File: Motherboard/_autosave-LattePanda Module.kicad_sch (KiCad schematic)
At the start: 73 parts, among them IC78 PCM2704CDBR, IC79 TS3DV621RUAR, J3 Conn_01x03_Pin, J5 SM03B-SRSS-TB, J78 Speaker_L, J79 Speaker_R, SW80 SW_Push, SW81 SW_Push, SW82 SW_Nidec_CAS-120A1, U10 ULC0524P, U11 ULC0524P, U12 ULC0524P, U84 PAM8403D, U88 RP2354B, Y1 ABM8-272-T3, Y2 ABM8-272-T3

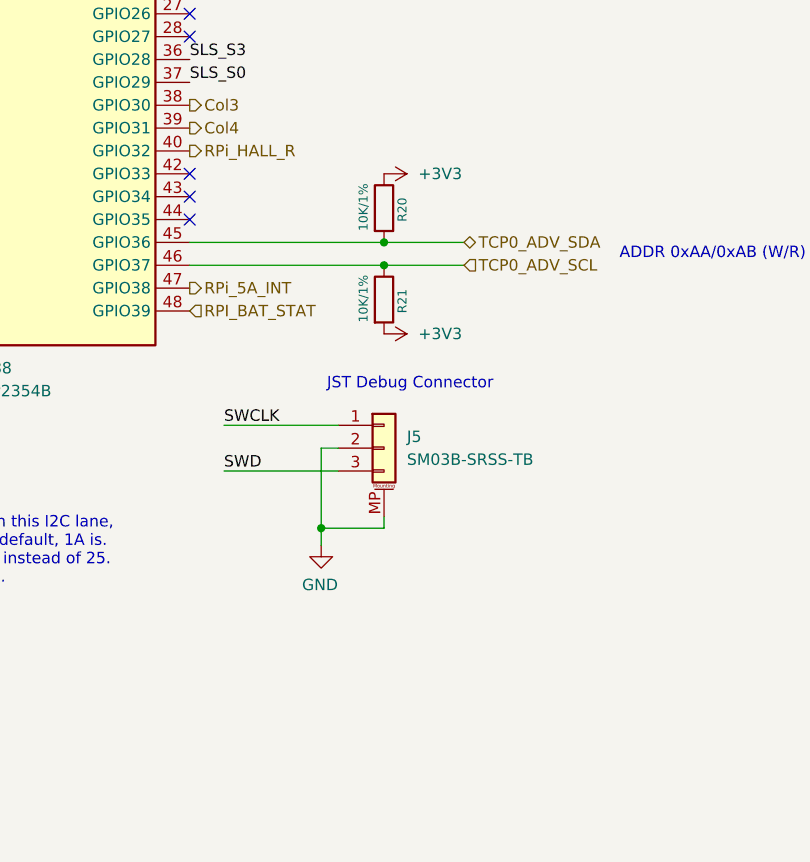
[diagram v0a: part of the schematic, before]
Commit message: Routed 1V8, 3V3 and 9V voltage regulators
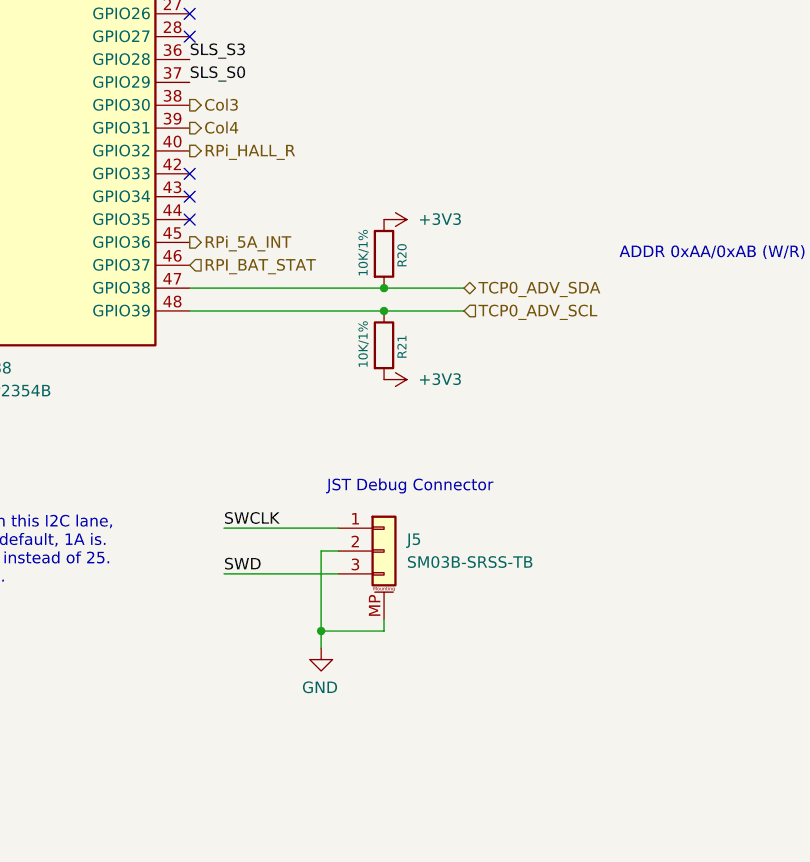
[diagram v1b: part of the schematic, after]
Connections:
- net RPI_BAT_STAT: now also U88.46 (GPIO37); no longer U88.48 (GPIO39)
- net RPi_5A_INT: now also U88.45 (GPIO36); no longer U88.47 (GPIO38)
- net TCP0_ADV_SCL: now also U88.48 (GPIO39); no longer U88.46 (GPIO37)
- net TCP0_ADV_SDA: now also U88.47 (GPIO38); no longer U88.45 (GPIO36)
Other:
- moved on the sheet: J5, R20, R21
